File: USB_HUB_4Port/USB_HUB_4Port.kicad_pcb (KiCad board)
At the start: 2 copper layers, 77.4 x 47.2 mm, 33 parts, among them J1 HOST USB, J2 USB_A_4, J3 USB_A_3, J4 USB_A_2, J5 USB_A_1, J6 Jack-DC, U1 GL852G, Y1 12Mhz

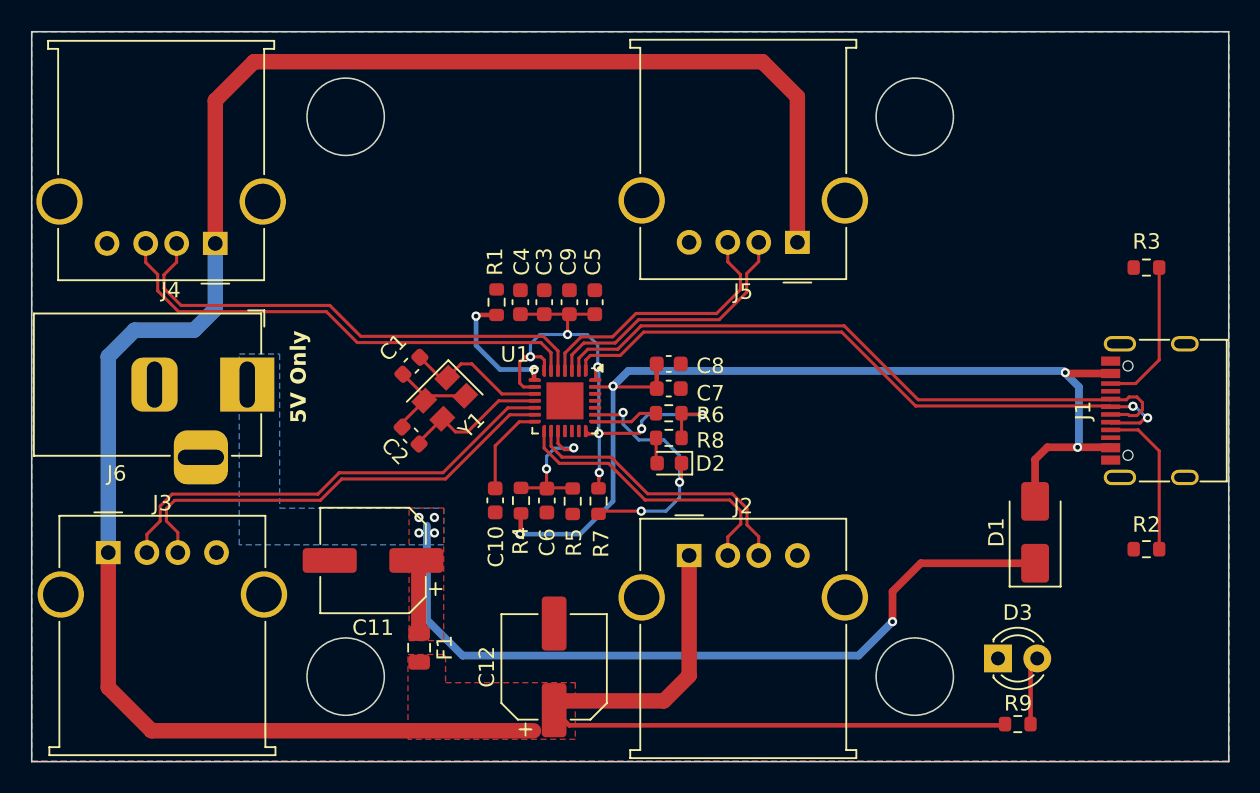
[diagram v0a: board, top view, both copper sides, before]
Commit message: Add project 4 hub usb
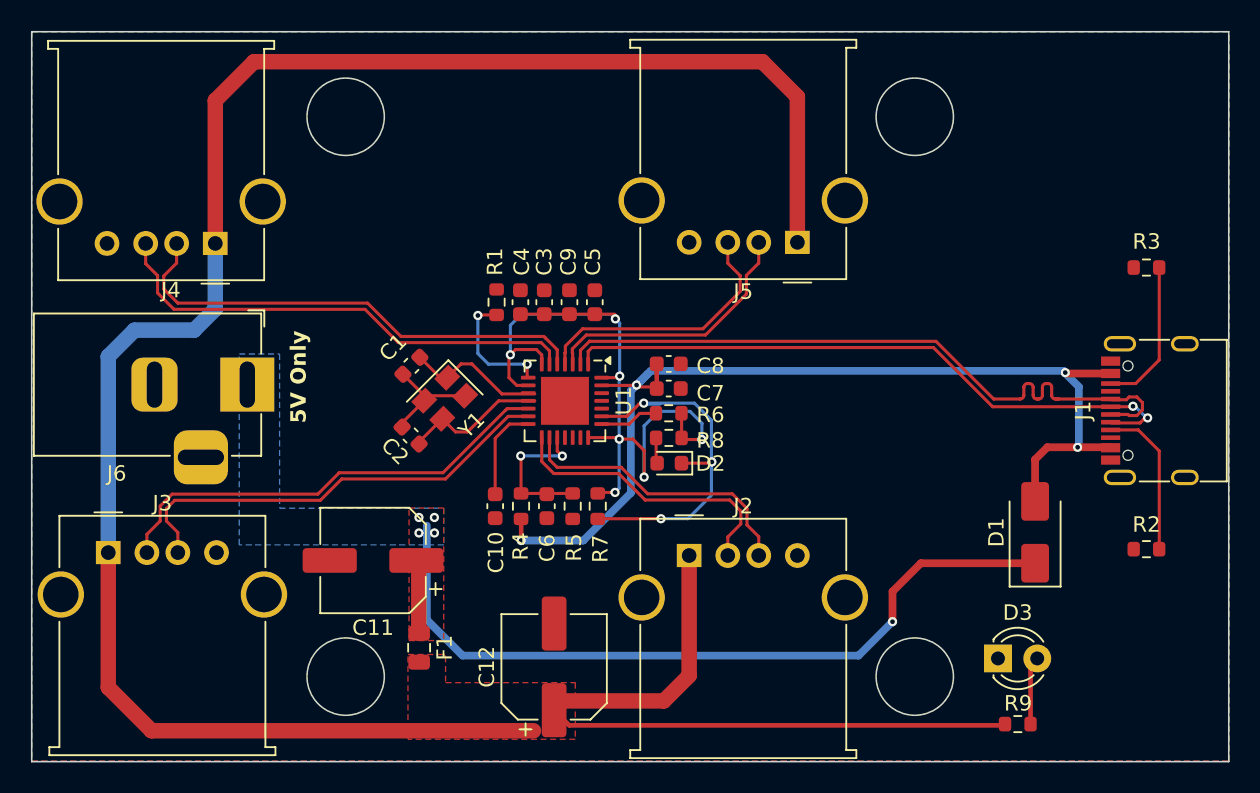
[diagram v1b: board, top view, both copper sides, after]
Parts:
- U1: footprint Package_DFN_QFN:QFN-28-1EP_4x4mm_P0.45mm_EP2.4x2.4mm -> Package_DFN_QFN:QFN-28-1EP_5x5mm_P0.5mm_EP3.1x3.1mm
- moved C10 0.38 mm to (77.8, 152.8)
- moved C6 0.37 mm to (81.1, 152.8)
- moved R4 0.36 mm to (79.4, 152.8)
- moved R7 0.33 mm to (84.4, 152.8)
- moved R5 0.32 mm to (82.8, 152.8)
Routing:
- net +3.3V: track 38.7 -> 52.7 mm
- net Net-(D2-K): track 16.8 -> 23.8 mm
- net Net-(U1-DP0): track 43.1 -> 45.0 mm
- net Net-(U1-DM0): track 42.6 -> 41.4 mm
- net Net-(D3-A): track 4.43 -> 3.81 mm
- net D2+: track 31.8 -> 31.3 mm
